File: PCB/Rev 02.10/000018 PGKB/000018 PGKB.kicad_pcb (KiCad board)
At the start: 4 copper layers, 93.5 x 72.5 mm, 154 parts, among them J1 USB C, J2 BM04B-SRSS-TB, U1 SN74HCS365PWR, U2 SN74HCS365PWR, U3 SN74HCS365PWR, U4 W25Q80DVSSIG, U5 RP2040, U6 MCP1825T-3302E/DC, U7 CAT811TTBI-GT3, Y1 12 MHz

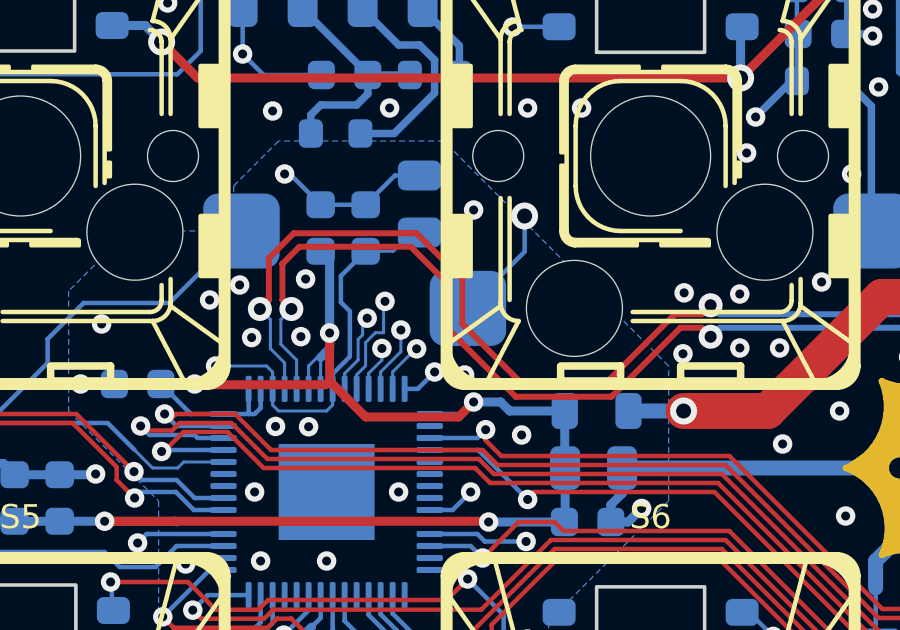
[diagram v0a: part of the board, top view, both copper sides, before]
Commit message: Updated layout from schematic
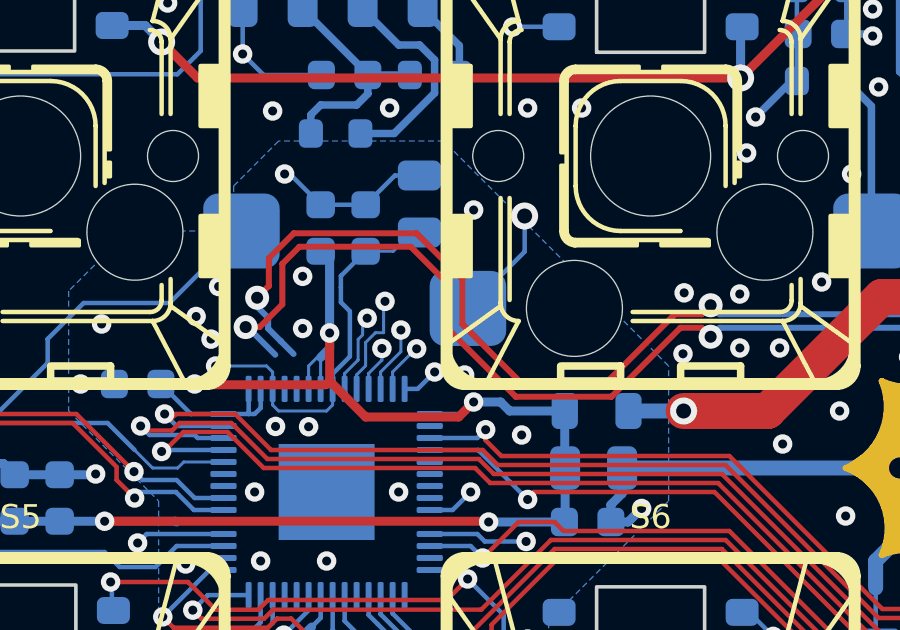
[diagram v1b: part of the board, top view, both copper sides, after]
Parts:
- R3, R4: value R_0603_10_5% -> 27
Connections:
- D11 pad 1: /Main/USB Connector/USB_D_N -> /Main/USB Connector/USB_D_P
- D11 pad 6: /Main/USB Connector/USB_D_P -> /Main/USB Connector/USB_D_N
- J1 pad A6: /Main/USB Connector/USB_D_N -> /Main/USB Connector/USB_D_P
- J1 pad A7: /Main/USB Connector/USB_D_P -> /Main/USB Connector/USB_D_N
- J1 pad B6: /Main/USB Connector/USB_D_N -> /Main/USB Connector/USB_D_P
- J1 pad B7: /Main/USB Connector/USB_D_P -> /Main/USB Connector/USB_D_N
- R3 pad 1: /Main/USB Connector/USB_D_P -> /Main/USB Connector/USB_D_N
- R3 pad 2: /Main/Microcontroller/USB_MCU_D_P -> /Main/Microcontroller/USB_MCU_D_N
- R4 pad 1: /Main/USB Connector/USB_D_N -> /Main/USB Connector/USB_D_P
- R4 pad 2: /Main/Microcontroller/USB_MCU_D_N -> /Main/Microcontroller/USB_MCU_D_P
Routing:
- net /Main/Microcontroller/USB_MCU_D_P: track 33.7 -> 32.3 mm

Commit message: routed all
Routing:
- net /Main/Microcontroller/USB_MCU_D_N: track 33.4 -> 34.6 mm
- net /Main/Microcontroller/USB_MCU_D_P: track 32.3 -> 33.5 mm
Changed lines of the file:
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@@
+	)
+	(segment
+		(start 67.1 125.2)
+		(end 67 125.1)
+		(width 0.15)
+		(layer "B.Cu")
+		(net 8)
 	)
 	(segment
@@
 		(end 66.151497 124.252316)
 		(width 0.2)
+		(layer "B.Cu")
+		(net 8)
+	)
+	(segment
+		(start 67.1 126.2625)
+		(end 67.1 125.2)
+		(width 0.15)
 		(layer "B.Cu")
 		(net 8)
@@
 	)
 	(segment
+		(start 66.7 125.437215)
+		(end 66.388604 125.125819)
+		(width 0.15)
+		(layer "B.Cu")
+		(net 9)
+	)
+	(segment
 		(start 88.9 124.225)
 		(end 81.199999 124.225001)
@@
 		(layer "B.Cu")
 		(net 9)
+	)
+	(segment
+		(start 66.7 126.2625)
+		(end 66.7 125.437215)
+		(width 0.15)
+		(layer "B.Cu")
+		(net 9)

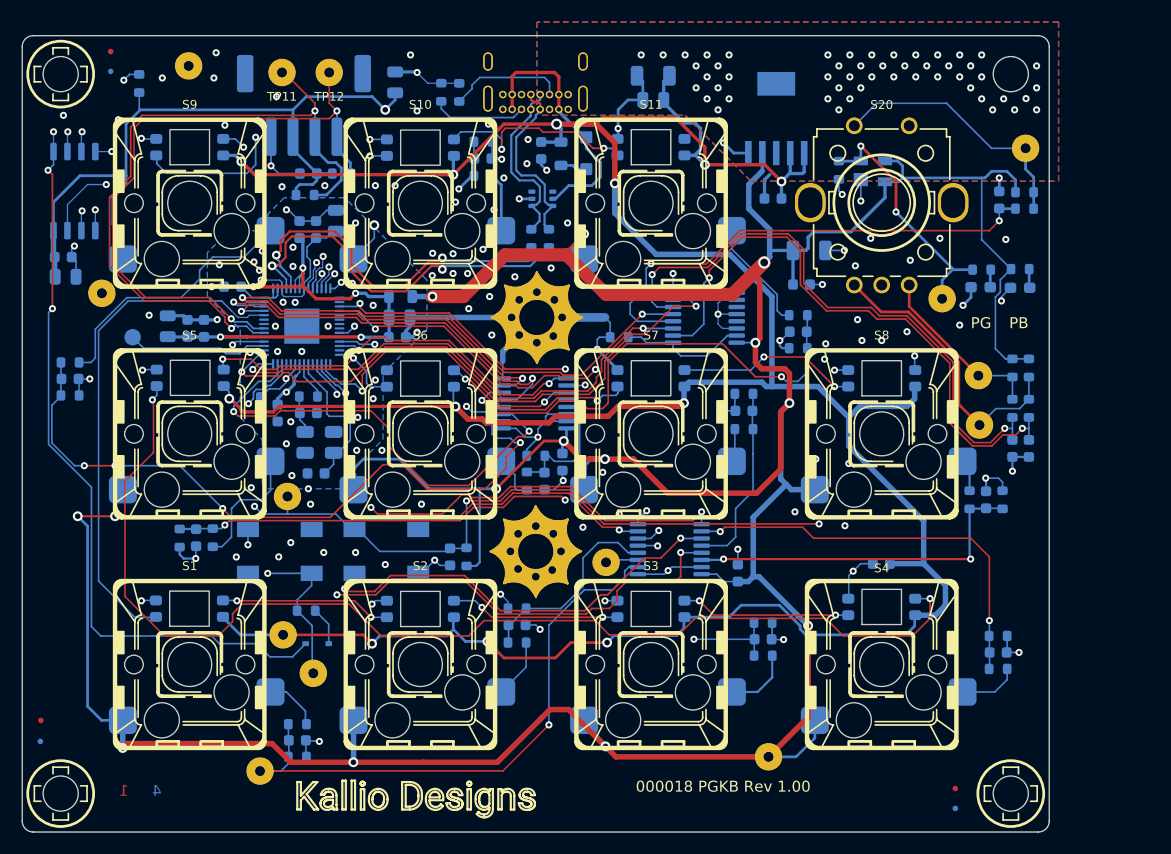
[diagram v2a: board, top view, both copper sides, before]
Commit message: Resolved DRC problems
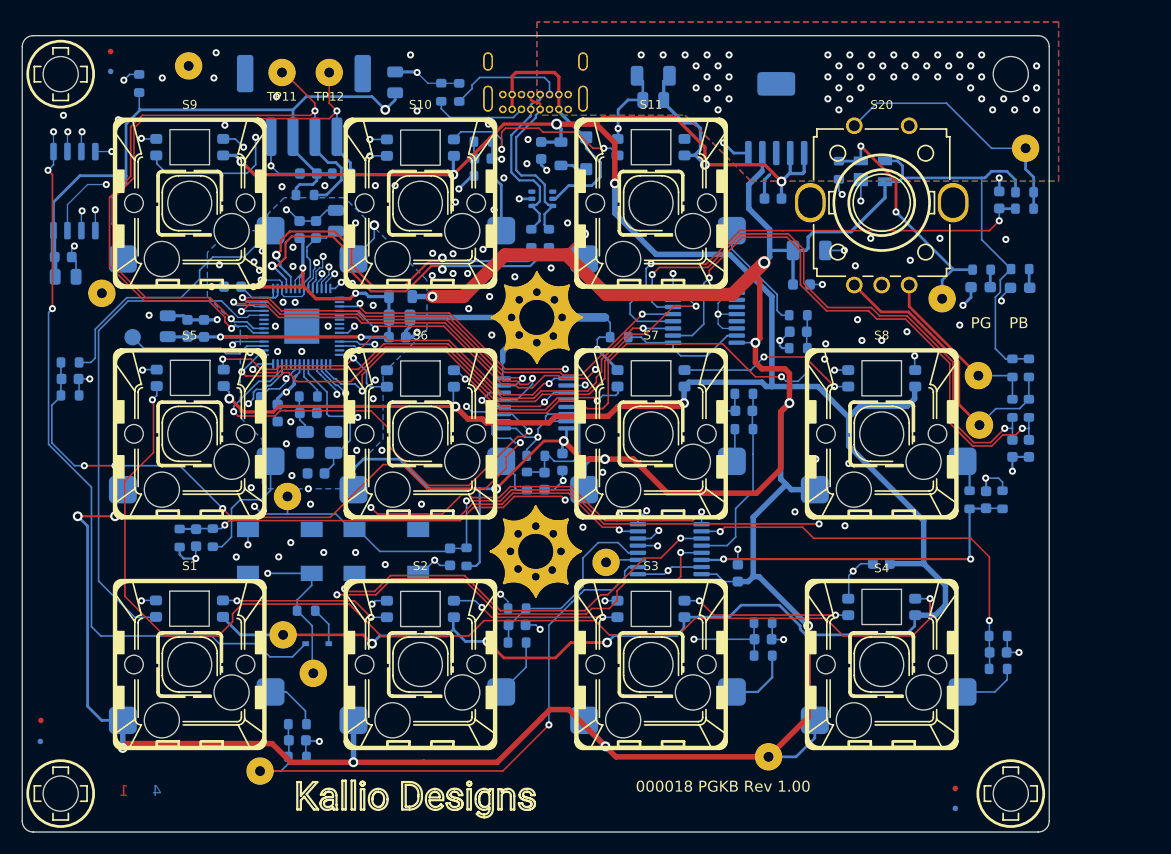
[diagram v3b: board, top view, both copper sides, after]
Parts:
- FB1, FB2: value Ferrite_500mA_TDK_MMZ2012Y152BT000 -> MMZ2012Y152BT000
- J2: value BM04B-SRSS-TB -> S4B-PH-SM4-TB
- R32, R33: value R_0603_360_1% -> 360
- S1, S10, S11, S2, S3, S4, S5, S6, S7, S8, S9: value 4954 -> 4958

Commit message: Test points for encoder signals
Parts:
- added TP10: TP D2.5 mm H0.9mm, KD_Connector_Pads:TestPoint_Pad_D2.5mm_H0.9mm, B.Cu at (143.8, 131.2)
- added TP17: TP D2.5 mm H0.9mm, KD_Connector_Pads:TestPoint_Pad_D2.5mm_H0.9mm, B.Cu at (143.9, 137.2)
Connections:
- J2 pad MP1: (no net) -> unconnected-(J2-PadMP1)
- J2 pad MP2: (no net) -> unconnected-(J2-PadMP2)

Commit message: Encoder Test points to layout
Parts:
- moved TP17 48.6 mm to (96.2, 128.3)
- moved TP10 35.5 mm to (108.4, 133.2)
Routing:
- net +3V3: track 437.1 -> 428.3 mm
- net /Main/Microcontroller/ENC_A: track 47.2 -> 55.5 mm, vias 2 -> 3
- net GND: track 163.8 -> 157.9 mm
- net /Main/Microcontroller/ENC_B: track 54.9 -> 60.1 mm
- net /Main/Neopixel LEDs/NEOPIXEL_VDD: track 288.7 -> 289.8 mm, vias 12 -> 13
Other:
- board text added: "BOOT"
- board text added: "RST"
